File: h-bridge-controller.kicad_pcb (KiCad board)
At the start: 2 copper layers, 98.8 x 55.1 mm, 104 parts, among them J1 Conn_02x03_Odd_Even, J2 Conn_01x04, Q1 IRF3205, Q10 BSS138, Q11 AO3401A, Q2 IRF3205, Q3 IRF3205, Q4 IRF3205, Q5 IRF3205, Q6 IRF3205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

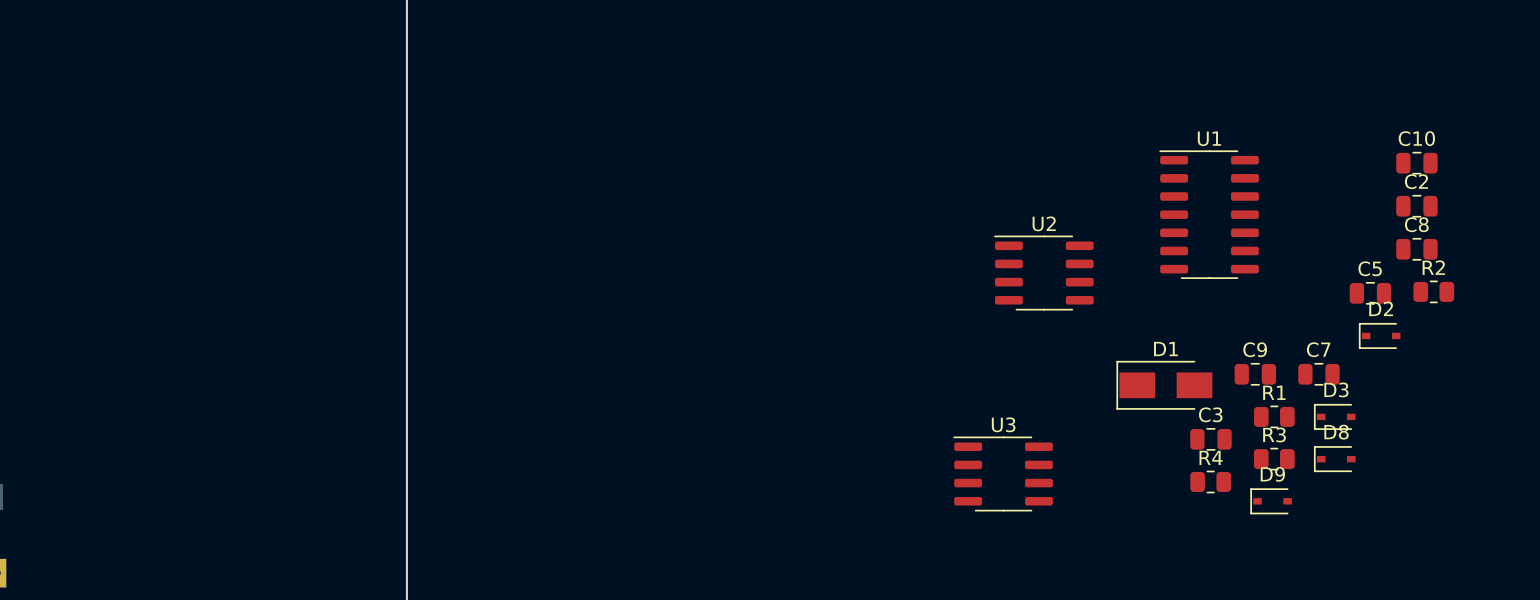
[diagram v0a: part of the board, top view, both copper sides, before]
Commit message: update to kicad6<< revert this
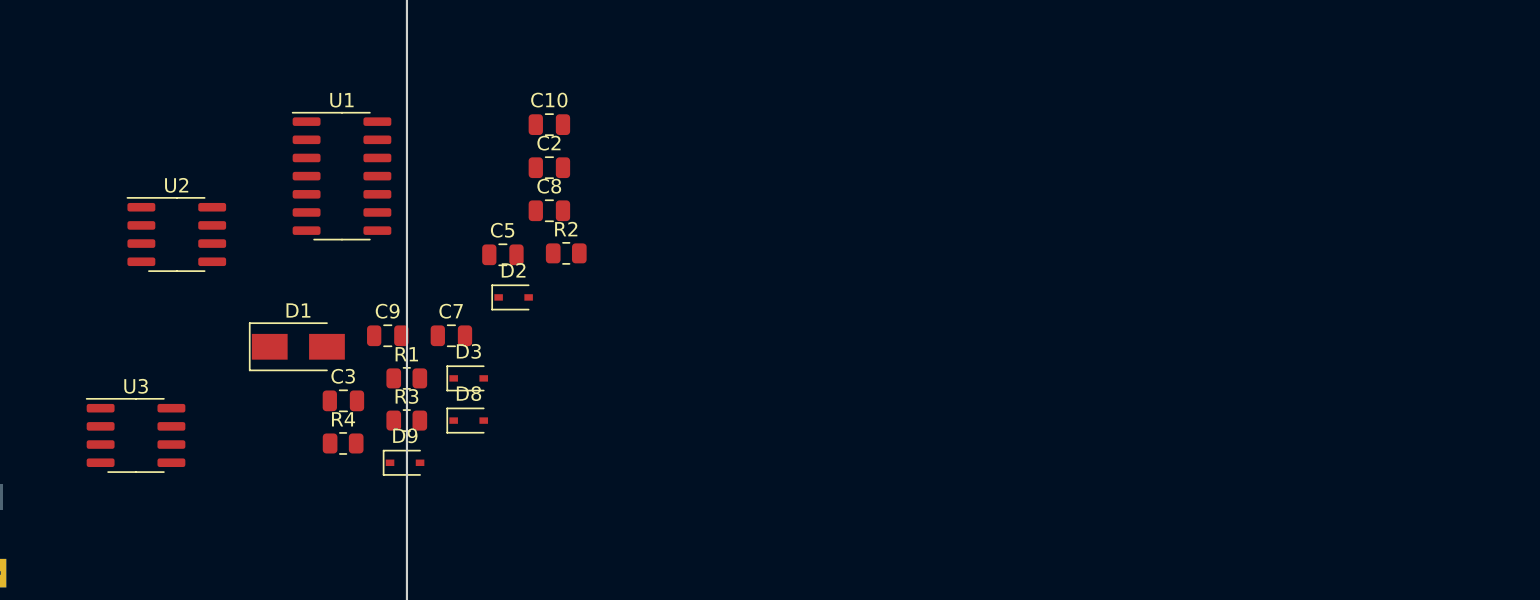
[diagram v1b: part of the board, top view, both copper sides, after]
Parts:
- moved C10 60.7 mm to (180.9, 63.1)
- moved C2 60.7 mm to (180.9, 66.1)
- moved C3 60.7 mm to (166.5, 82.4)
- moved C5 60.7 mm to (177.7, 72.2)
- moved C7 60.7 mm to (174.1, 77.9)
- moved C8 60.7 mm to (180.9, 69.2)
- moved C9 60.7 mm to (169.6, 77.9)
- moved D1 60.7 mm to (163.3, 78.7)
- moved D2 60.7 mm to (178.4, 75.2)
- moved D3 60.7 mm to (175.3, 80.9)
- moved D8 60.7 mm to (175.3, 83.8)
- moved D9 60.7 mm to (170.8, 86.8)
- moved R1 60.7 mm to (170.9, 80.9)
- moved R2 60.7 mm to (182.1, 72.1)
- moved R3 60.7 mm to (170.9, 83.8)
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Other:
- net class Default removed

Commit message: Revert "update to kicad6<< revert this"
This reverts commit 94c354bf1f03422d884be196bd183532f7be4acb.
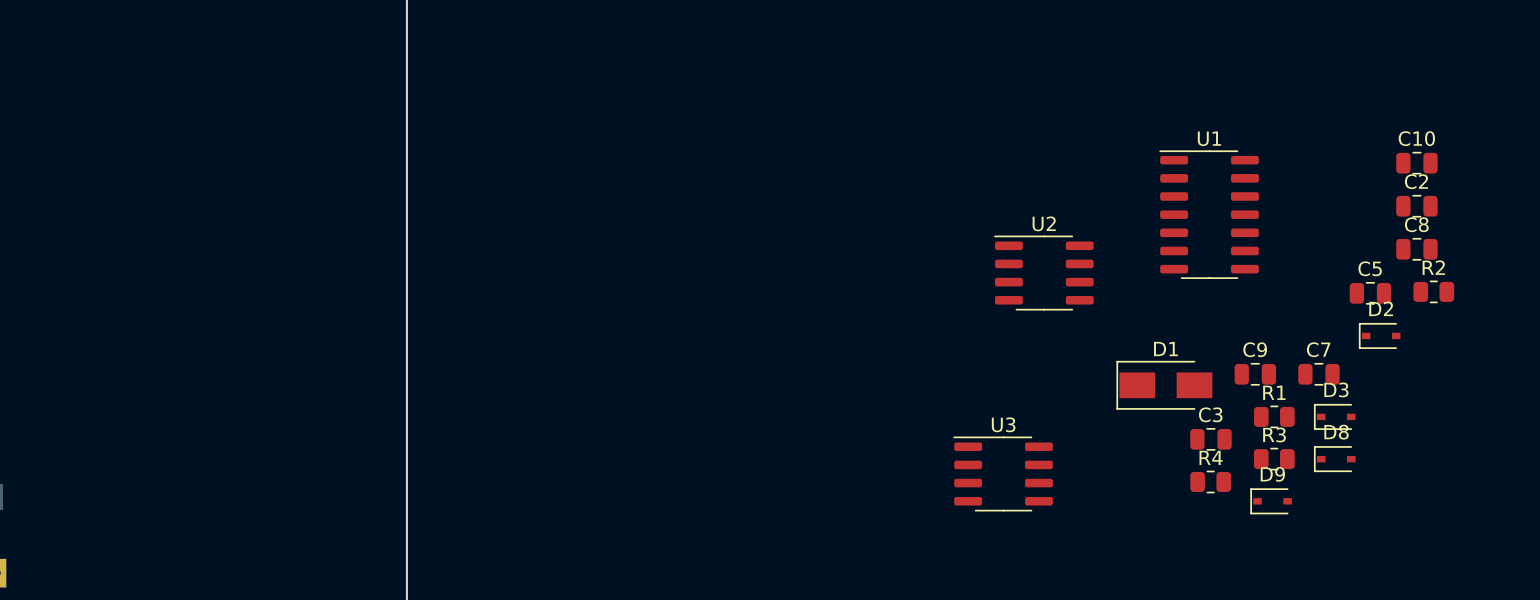
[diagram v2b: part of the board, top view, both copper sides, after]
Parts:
- moved C10 60.7 mm to (241.6, 65.8)
- moved C2 60.7 mm to (241.6, 68.8)
- moved C3 60.7 mm to (227.2, 85.1)
- moved C5 60.7 mm to (238.3, 74.9)
- moved C7 60.7 mm to (234.7, 80.6)
- moved C8 60.7 mm to (241.6, 71.8)
- moved C9 60.7 mm to (230.3, 80.6)
- moved D1 60.7 mm to (224.0, 81.4)
- moved D2 60.7 mm to (239.1, 77.9)
- moved D3 60.7 mm to (235.9, 83.6)
- moved D8 60.7 mm to (235.9, 86.5)
- moved D9 60.7 mm to (231.5, 89.5)
- moved R1 60.7 mm to (231.6, 83.6)
- moved R2 60.7 mm to (242.7, 74.8)
- moved R3 60.7 mm to (231.6, 86.5)
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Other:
- net class Default added: clearance 0.2, trace_width 0.25, via_dia 0.6, via_drill 0.3
